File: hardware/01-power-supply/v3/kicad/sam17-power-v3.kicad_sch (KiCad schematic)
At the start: 107 parts, among them J1 12VAC CT 2A, J2 BUS -12/G/G/+12, J3 AC 230V IN, J4 TR1 pri (ext), J5 CHASIS, J6 +5V/RTN, J7 SMPS 230V TAP, J8 I2C AISLADO, U1 LM2941CT/NOPB, U10 ADS1115 0x49, U11 TMP1075 0x48, U12 ISO1541, U2 LM2991T/NOPB, U3 LM7805, U4 LT3045EDD#TRPBF, U5 LT3045EDD#TRPBF, U6 LT3094EDD#PBF, U7 LT3094EDD#PBF, U8 INA226 0x40, U9 INA226 0x41

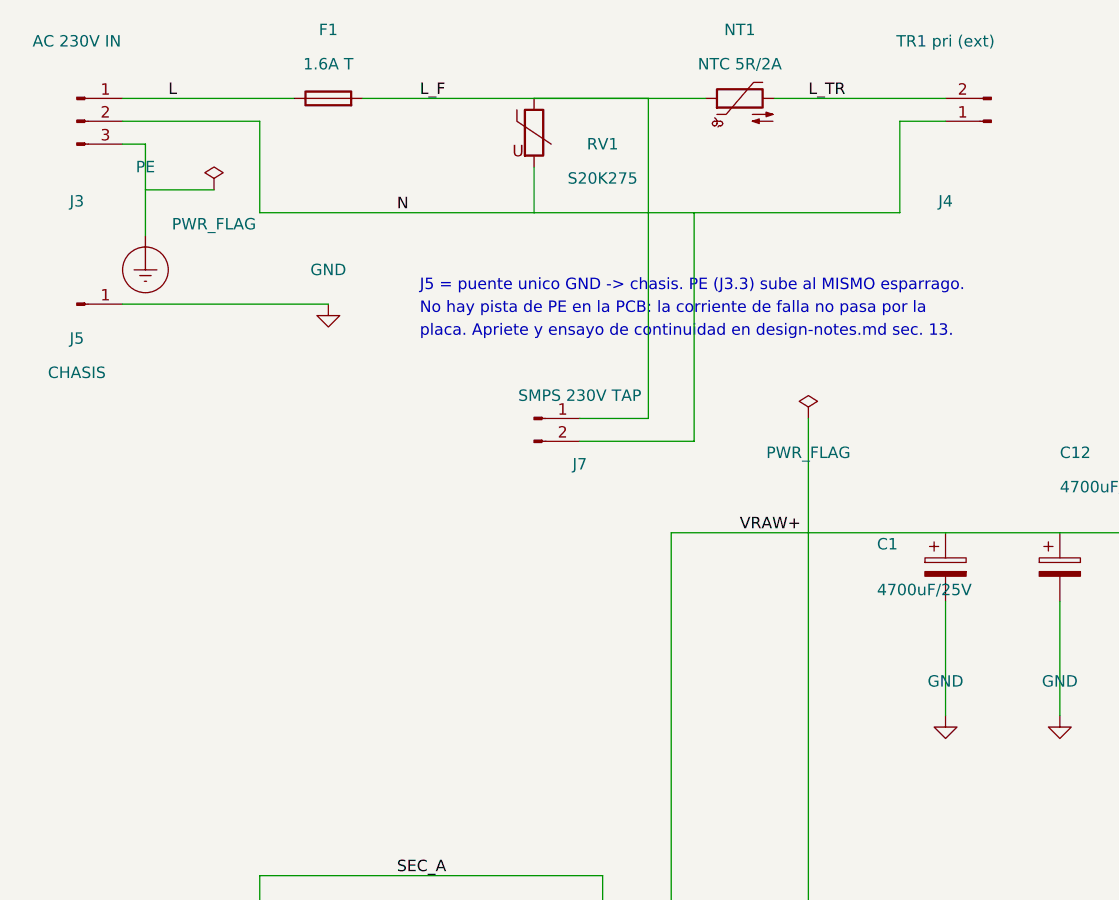
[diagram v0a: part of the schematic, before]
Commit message: El filtro de la SMPS entra en la placa, y ensena que un componente serie no puede ir sin poblar
Samuel eligio pedir presupuesto de la pantalla y meter la huella del filtro
mientras tanto. Al meterla salio que "huella" no era la palabra para la mitad de
ella.

L1 esta EN SERIE con la alimentacion de la SMPS. Un componente serie no puede ir
DNP: sin poblar, la SMPS se queda sin red. O va puesto o hay que puentearlo, y un
puente de 230 V a 0,2 A no es un net tie. Va poblado. Su inductancia de fuga es
despreciable a 50 Hz para 0,2 A.

CY1/CY2 estan EN PARALELO, asi que su ausencia no rompe nada y si pueden esperar.
Esperan por un numero que este repo no puede acotar: 2 x 1 nF anaden 145 uA de
fuga a tierra a 230 V/50 Hz, y el limite esta en la clausula de IEC 62368-1 que
13.4 ya declino citar por ser de pago. Se pueblan con la medida del bring-up
delante.

Y la aritmetica dice algo incomodo. A 65 kHz el choke de 10 mH son 4,1 kOhm y la
capacidad entre devanados del toroide unos 12 kOhm: solo el choke deja pasar el
75 % de la corriente al toroide. Con dos caps Y de 1 nF baja al 7 %. El choke
solo es teatro -- sube la impedancia de un camino que ya era de alta impedancia.
Lo que hace el trabajo es el retorno local corto.

Eso refuerza la pantalla en vez de sustituirla: la pantalla no reparte la
corriente, quita el camino. El filtro de J7 es un seguro contra que la pantalla
no llegue o no baste.

El choke pincha en L_F, entre F1 y NT1, y la puerta de netlist lo vigila: la
regla de la spec v2 §7 es que la SMPS comparte fusible con el toroide pero NO
comparte el limitador de inrush, que esta dimensionado para TR1.

El golden de conectividad hizo justo su trabajo: 10 lineas de diferencia, y las
diez son las que se esperaban. J7 sale de L_F y N, entra en L_SMPS y N_SMPS a
traves de L1, y PE gana las dos Y. Nada mas se movio.

Co-Authored-By: Claude Opus 5 (1M context) <noreply@anthropic.com>
Claude-Session: https://claude.ai/code/session_011RDHu5geUcqfND7jYruVeF
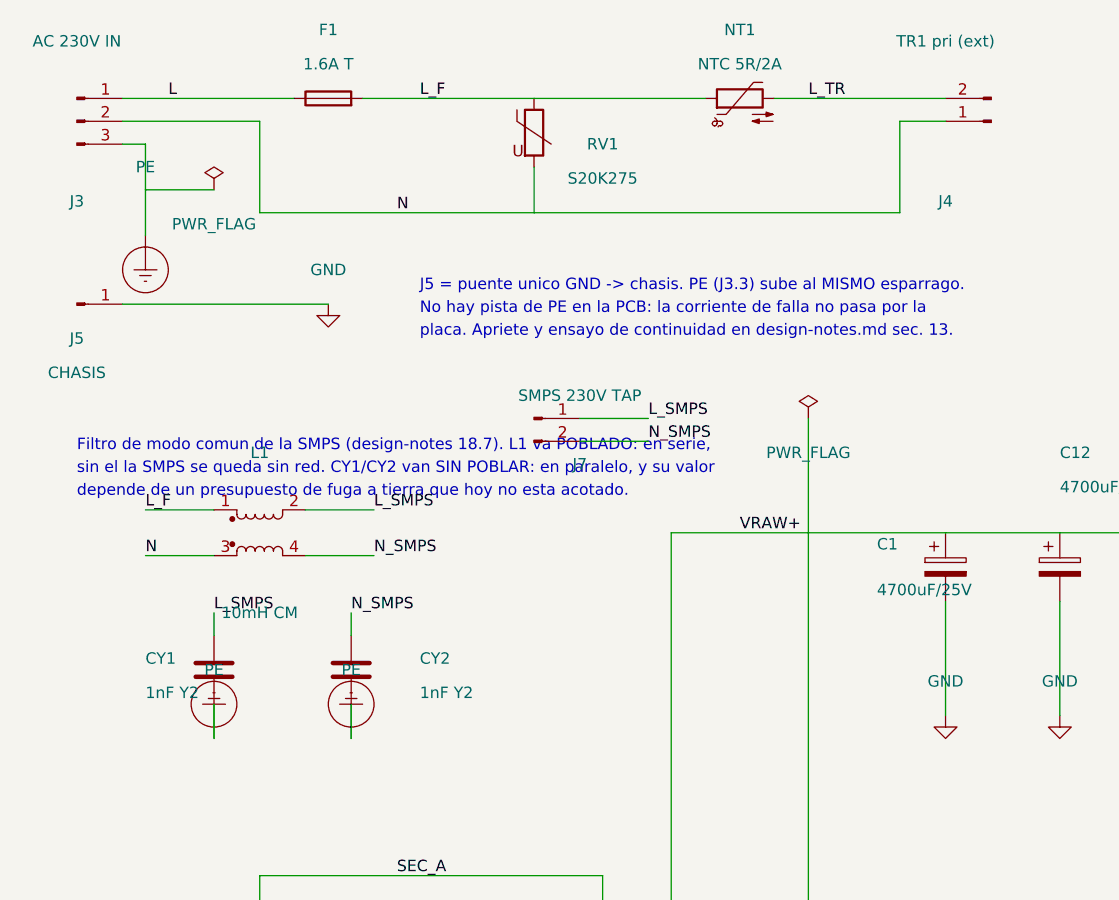
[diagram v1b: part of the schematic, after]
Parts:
- added CY1, CY2: 1nF Y2, Capacitor_THT:C_Disc_D10.5mm_W5.0mm_P7.50mm, symbol Device:C
- added L1: 10mH CM, Inductor_THT:L_CommonMode_Toroid_Vertical_L30.5mm_W15.2mm_Px10.16mm_Py20.32mm_Bourns_8100, symbol Device:L_Coupled
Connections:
- net L_F: now also L1.1; no longer J7.1 (Pin_1)
- net N: now also L1.3; no longer J7.2 (Pin_2)
- net PE: now also CY1.2, CY2.2
- new net L_SMPS: CY1.1, J7.1 (Pin_1), L1.2
- new net N_SMPS: CY2.1, J7.2 (Pin_2), L1.4
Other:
- note added: "Filtro de modo comun de la SMPS (design-notes 18.7). L1 va POBLADO: en serie,"
- note added: "depende de un presupuesto de fuga a tierra que hoy no esta acotado."
- note added: "sin el la SMPS se queda sin red. CY1/CY2 van SIN POBLAR: en paralelo, y su valor"

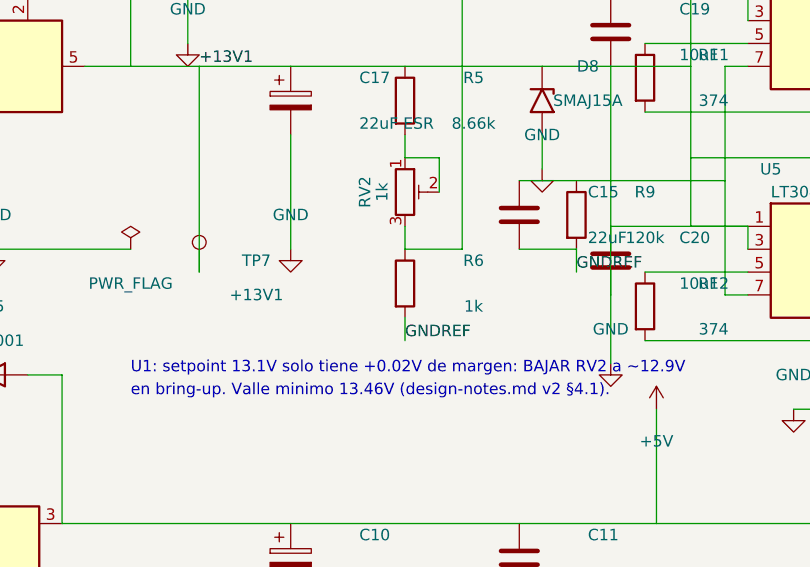
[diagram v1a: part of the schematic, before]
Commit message: R6 estaba dibujado espejado de R8, y su pad de referencia nunca estuvo conectado
DRC real: 0 infracciones, 0 elementos sin conectar. Todas las puertas propias
en verde, incluida `revisar_isla_referencia()`, que era la ultima en rojo.

## El hallazgo

R6 y R8 son el mismo divisor de ajuste a cada lado de la placa, con la misma
huella y la misma colocacion. En el esquematico estan dibujados espejados --
R6 lleva GNDREF abajo y R8 arriba -- asi que el pin que toca la referencia es
el 2 en uno y el 1 en el otro.

En la PLACA eso manda el pad de GNDREF de R6 a x=57.16. ISLA_REF acaba en
x=54: ni la zona lo alcanzaba ni una pista puede llegar sin sacar la
referencia de su isla. **R6.2 no ha estado conectado en ninguna version de
esta fuente**, y R6 es el fondo del divisor de ajuste de U1, el pre-regulador
de +12 V.

No se vio antes porque la puerta que lo vigila solo mira PISTAS de GNDREF, y
hasta esta tanda no habia ninguna: era verde por vacia. Es el Principio VIII
de la constitucion aplicandose solo -- una comprobacion que nunca se ha visto
fallar no es una comprobacion.

## El arreglo

Girar el simbolo de R6 180 grados. El cableado del esquematico no se mueve ni
un milimetro y la huella tampoco -- un resistor es simetrico -- pero el pad
que lleva GNDREF pasa a ser el 1, que esta en x=47 y dentro de la isla, igual
que el de R8.

El golden lo caza y por eso existe:

    -GNDREF:        C15-2 C16-2 JP1-1 R10-2 R6-2 R8-1 R9-2
    +GNDREF:        C15-2 C16-2 JP1-1 R10-2 R6-1 R8-1 R9-2
    -Net-(U1-ADJ):  R6-1 RV2-3 U1-1
    +Net-(U1-ADJ):  R6-2 RV2-3 U1-1

Dos lineas, y ninguna otra red se movio.

## Estado de las puertas

    check_netlist.py   OK -- shunts en serie, tres divisores en su sentido,
                       los cinco chips en el I2C, barrera de masas sin un
                       nodo comun
    check_bom.py       OK -- 110 en la hoja, 114 designadores
    netdiff            golden actualizado, solo estas dos redes
    DRC (kicad-cli)    0 infracciones, 0 sin c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
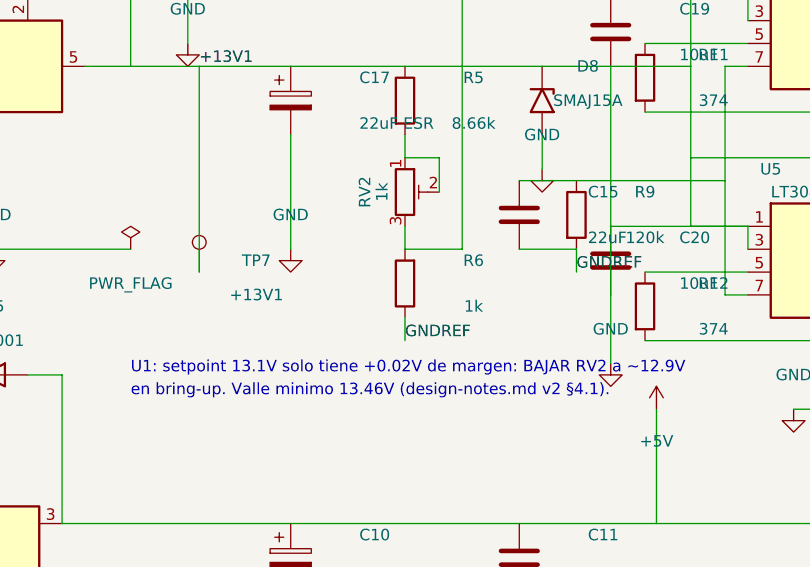
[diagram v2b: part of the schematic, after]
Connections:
- net GNDREF: now also R6.1; no longer R6.2
- net at RV2.3, U1.1 (ADJ): now also R6.2; no longer R6.1

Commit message: Dos fusibles en serie en el mismo primario, y ninguno sabia cual miraba
Cierra la parte del #130 que tocaba la PCB. `F1` sale de la placa: el fusible
de red se queda en el IEC C14 de la pared del recinto.

## El desfase

La spec del case §7 lo dice desde el principio, dos veces -- "entrada IEC C14
con portafusible + interruptor" -- y `F1` estaba ademas en la placa. Nadie
habia cruzado los dos documentos. Dos fusibles en serie en el mismo primario
es peor que uno solo: el mismo fallo los ve a los dos y no hay forma de saber
cual miro.

Se queda el del IEC porque es el ACCESIBLE. Cambiar `F1` obligaba a abrir un
recinto de acero cerrado.

**El requisito no se va con la pieza**, y eso queda escrito en design-notes
§14.2 y en el README de fab: el fusible del chasis tiene que ser 1.6 A lento
-- por el inrush del toroide de 120 VA mas los 0.2 A de la SMPS -- y su
portafusible **cerrado**, que es lo que pide haber elegido aislamiento
reforzado. Si el IEC que se compre no cumple las dos, no vale: la placa ya no
tiene red detras.

## Lo que cambia

    redes            60 -> 59   (`L` y `L_F` eran el mismo nodo sin F1 en medio)
    nodos           303 -> 301
    pads de red      23 -> 19   (los cuatro clips del portafusible)
    DRC               0 infracciones, 0 sin conectar
    las 7 puertas     en verde

`L_F` significaba "L despues del fusible" y aqui ya no hay fusible: lo que
entra por J3 es `L`, sin mas. El invariante de `check_netlist.py` se reescribe
contra ese nombre y sigue vigilando LO MISMO -- de que nodo cuelga el choke de
la SMPS: antes de NT1, porque el limitador esta dimensionado para TR1 y la
SMPS no debe compartirlo (spec v2 §7).

## Y una regla que medía la serigrafía

Al re-rutear salio que `revisar_diagonal()` habia bajado de 40 a 32 mm sobre
un umbral de 30. La causa no era electrica: `bbox_de()` usaba
`GetBoundingBox()` a secas, que **cuenta el texto**, y en la ronda anterior yo
habia movido la referencia "C2" por un choque de serigrafia. Ocho milimet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
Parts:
- removed F1: 1.6A T, Fuse:Fuseholder_Cylinder-5x20mm_Schurter_FPG4_Vertical_Closed, symbol Device:Fuse
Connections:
- net L_F is gone; now on net L: L1.1, NT1.1, RV1.1

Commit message: La placa regenerada con las huellas buenas, y un literal que dependia de una
NT1 movio un pad 2,4 mm al pasar a su huella real (paso 5,1 y no 7,5), asi que
esto es esquematico, netlist, placa, relleno de zona y las siete salidas de
fabricacion otra vez.

Y saco a la luz una cota escrita dos veces: el 95.5 de rutear_red() era la x
del pad 2 CON LA HUELLA VIEJA. Al mover el paso, la subida de NT1.2 arrancaba
en el aire. Ahora se pide con pad_xy(), como sus dos vecinos de arriba -- un
literal que depende de una huella es la misma cota en dos sitios, y solo uno
de los dos se entera cuando cambia.

  DRC (kicad-cli, --severity-all)   0 infracciones  0 sin conectar  0 paridad
  ruteo                             1024 segmentos (antes 1033), 176 vias
  netdiff                           VERDE -- la conectividad no se movio
  barrera de red                    10,63 mm entre pads
                                     7,99 mm sobre el cobre del gerber
  zona GNDREF en el gerber          2159 mm2 de cobre relleno
  cpl                               42 designadores, ninguno con rotacion != 0

El .drl cambia en tres sitios y por eso habia que reexportarlo: el MOV pasa de
1,1 a 1,3, el faston de 1,6 a 1,3 y el NTC de 1,1 a 0,8. Un taladro solo
existe en el drill: el .kicad_pcb no se manda a fabricar.

Co-Authored-By: Claude Sonnet 5 <noreply@anthropic.com>
Claude-Session: https://claude.ai/code/session_01B8kQ36zt3gJuqVVwrKaJzk
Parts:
- NT1: footprint sam17:NTC_Disc_D11.5mm_W4.5mm_P7.5mm -> sam17:NTC_Disc_D10.0mm_W4.0mm_P5.1mm
